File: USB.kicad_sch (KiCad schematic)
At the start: 8 parts, among them J3 USB-C_GCT_USB4145-03-0070-C, U11 TPD4E05U06QDQARQ1

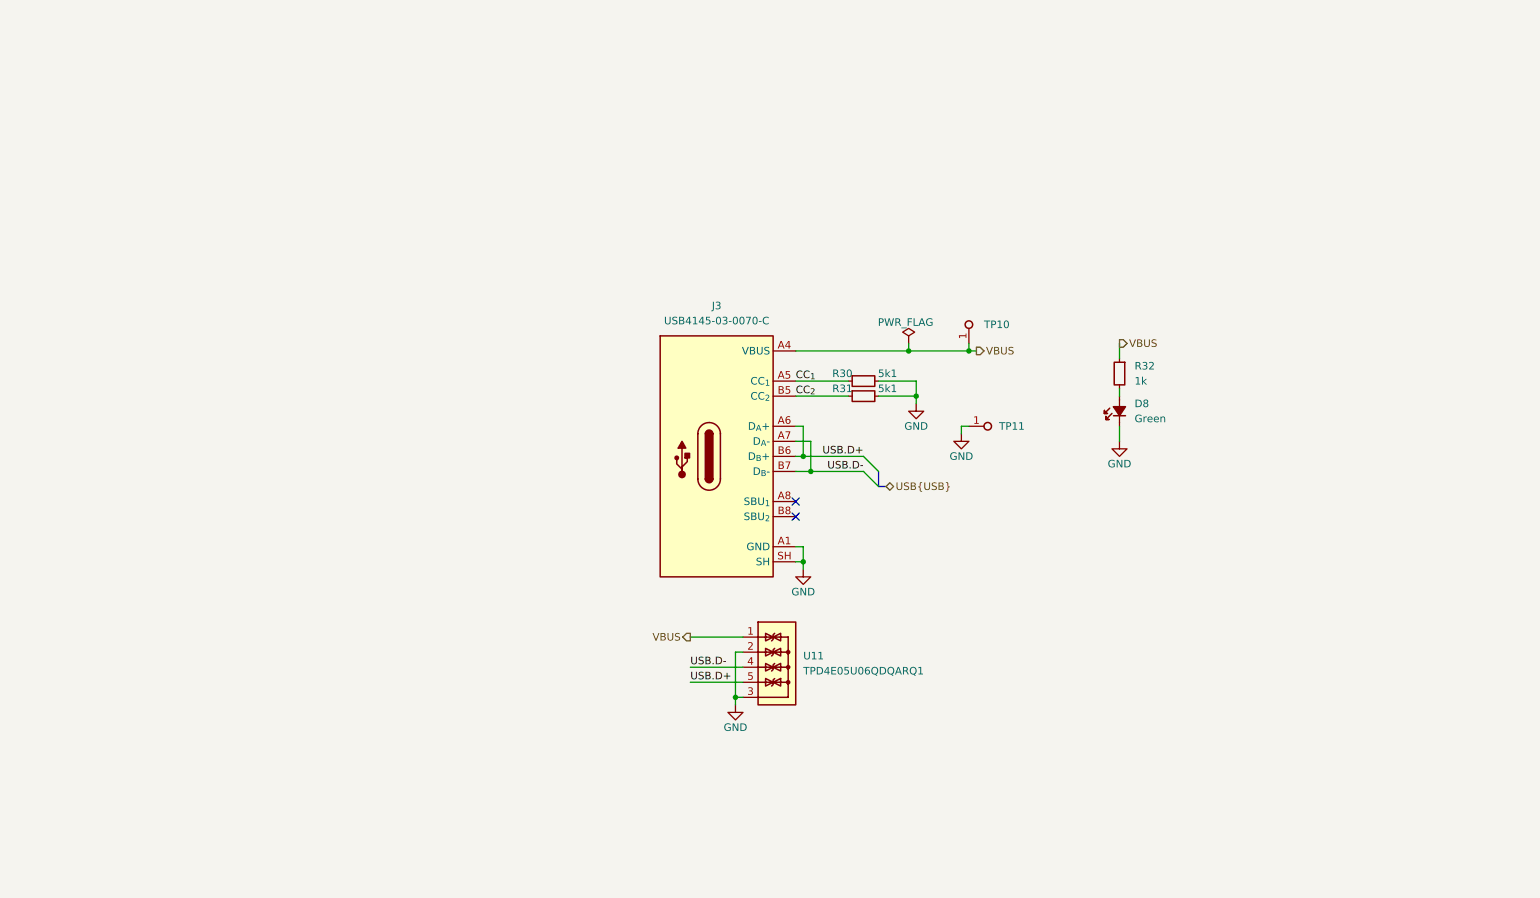
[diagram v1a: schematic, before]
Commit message: [#72133] Update USB FTDI sheet
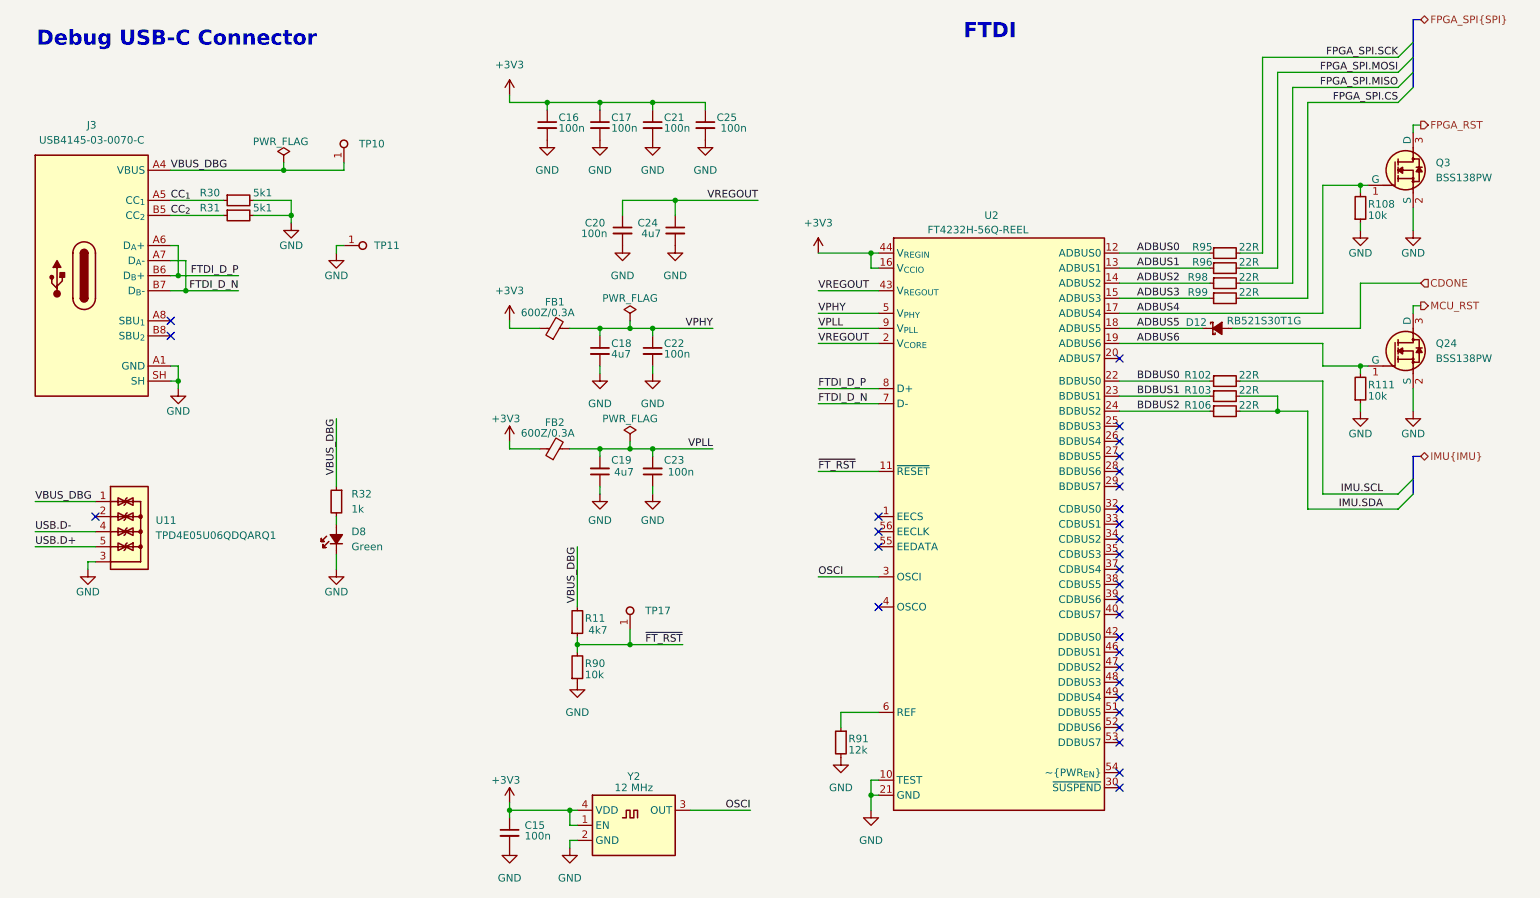
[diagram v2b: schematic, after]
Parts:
- added C15, C16, C17, C20, C21, C22, C23, C25: C_100n_16V_X7R_0402, antmicro-footprints:C_0402_1005Metric, symbol antmicroCapacitors0402:C_100n_16V_X7R_0402
- added C18, C19, C24: C_4u7_0402, antmicro-footprints:C_0402_1005Metric, symbol antmicroCapacitors0402:C_4u7_0402
- added D12: RB521S30T1G, antmicro-footprints:SOD-523, symbol antmicroDiodesRectifiersSingle:RB521S30T1G
- added FB1, FB2: FB_600Z_0.3A_Murata-BLM15AG_0402, antmicro-footprints:FB_0402_1005Metric, symbol antmicroFerriteBeadsandChips:FB_600Z_0.3A_Murata-BLM15AG_0402
- added Q24, Q3: BSS138PW, antmicro-footprints:SC70-3, symbol antmicroTransistorsFETsMOSFETsSingle:BSS138PW
- added R102, R103, R106, R95, R96, R98, R99: R_22R_0402, antmicro-footprints:R_0402_1005Metric, symbol antmicroResistors0402:R_22R_0402
- added R108, R111, R90: R_10k_0402, antmicro-footprints:R_0402_1005Metric, symbol antmicroResistors0402:R_10k_0402
- added R11: R_4k7_0402, antmicro-footprints:R_0402_1005Metric, symbol antmicroResistors0402:R_4k7_0402
- added R91: R_12k_0402, antmicro-footprints:R_0402_1005Metric, symbol antmicroResistors0402:R_12k_0402
- added TP17: TP_0.75mm_SMD, antmicro-footprints:TP_SMD_0.75mm, symbol antmicroTestPoints:TP_0.75mm_SMD
- added U2: FT4232H_VQFN, antmicro-footprints:QFN-56-1EP_8x8mm_P0.5mm, symbol antmicroInterfaceControllers:FT4232H_VQFN
- added Y2: Oscillator_12MHz_ASFLMB, antmicro-footprints:Oscillator_SMD_Abracon_ASFLMB_5x3.2x0.85mm, symbol antmicroOscillators:Oscillator_12MHz_ASFLMB
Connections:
- net GND: now also C15.2, C16.2, C17.2, C18.2, C19.1, C20.2, C21.2, C22.2, C23.1, C24.2, C25.2, Q24.2 (S), Q3.2 (S), R108.1, R111.1, R90.1, R91.2, U2.10 (TEST), U2.21 (GND), U2.41 (GND), U2.45 (GND), U2.57 (GND), Y2.2 (GND); no longer U11.2, U11.9
- net USB.D+: no longer J3.A6 (D_{A}+), J3.B6 (D_{B}+)
- net USB.D-: no longer J3.A7 (D_{A}-), J3.B7 (D_{B}-)
- net VBUS renamed VBUS_DBG
- net VBUS_DBG: now also R11.2
- new net: R91.1, U2.6 (REF)
- new net: U11.2, U11.9
- new net +3V3: C15.1, C16.1, C17.1, C21.1, C25.1, FB1.1, FB2.1, U2.16 (V_{CCIO}), U2.36 (V_{CCIO}), U2.44 (V_{REGIN}), U2.50 (V_{CCIO}), Y2.1 (EN), Y2.4 (VDD)
- new net ADBUS0: R95.1, U2.12 (ADBUS0)
- new net ADBUS1: R96.1, U2.13 (ADBUS1)
- new net ADBUS2: R98.1, U2.14 (ADBUS2)
- new net ADBUS3: R99.1, U2.15 (ADBUS3)
- new net ADBUS4: Q3.1 (G), R108.2, U2.17 (ADBUS4)
- new net ADBUS5: D12.1 (C), U2.18 (ADBUS5)
- new net ADBUS6: Q24.1 (G), R111.2, U2.19 (ADBUS6)
- new net BDBUS0: R102.1, U2.22 (BDBUS0)
- new net BDBUS1: R103.1, U2.23 (BDBUS1)
- new net BDBUS2: R106.1, U2.24 (BDBUS2)
- new net CDONE: D12.2 (A)
- new net FPGA_RST: Q3.3 (D)
- new net FPGA_SPI.CS: R99.2
- new net FPGA_SPI.MISO: R98.2
- new net FPGA_SPI.MOSI: R96.2
- new net FPGA_SPI.SCK: R95.2
- new net FTDI_D_N: J3.A7 (D_{A}-), J3.B7 (D_{B}-), U2.7 (D-)
- new net FTDI_D_P: J3.A6 (D_{A}+), J3.B6 (D_{B}+), U2.8 (D+)
- new net IMU.SCL: R102.2
- new net IMU.SDA: R103.2, R106.2
- new net MCU_RST: Q24.3 (D)
- new net OSCI: U2.3 (OSCI), Y2.3 (OUT)
- new net VPHY: C18.1, C22.1, FB1.2, U2.5 (V_{PHY})
- new net VPLL: C19.2, C23.2, FB2.2, U2.9 (V_{PLL})
- new net VREGOUT: C20.1, C24.1, U2.2 (V_{CORE}), U2.31 (V_{CORE}), U2.43 (V_{REGOUT})
- new net ~{FT_RST}: R11.1, R90.2, TP17.1, U2.11 (~{RESET})
- no-connect marks 2 -> 31
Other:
- note added: "Debug USB-C Connector"
- note added: "FTDI"
- moved on the sheet: D8, J3, R30, R31, R32, TP10, TP11, U11

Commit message: [#72133] Update USB sheets
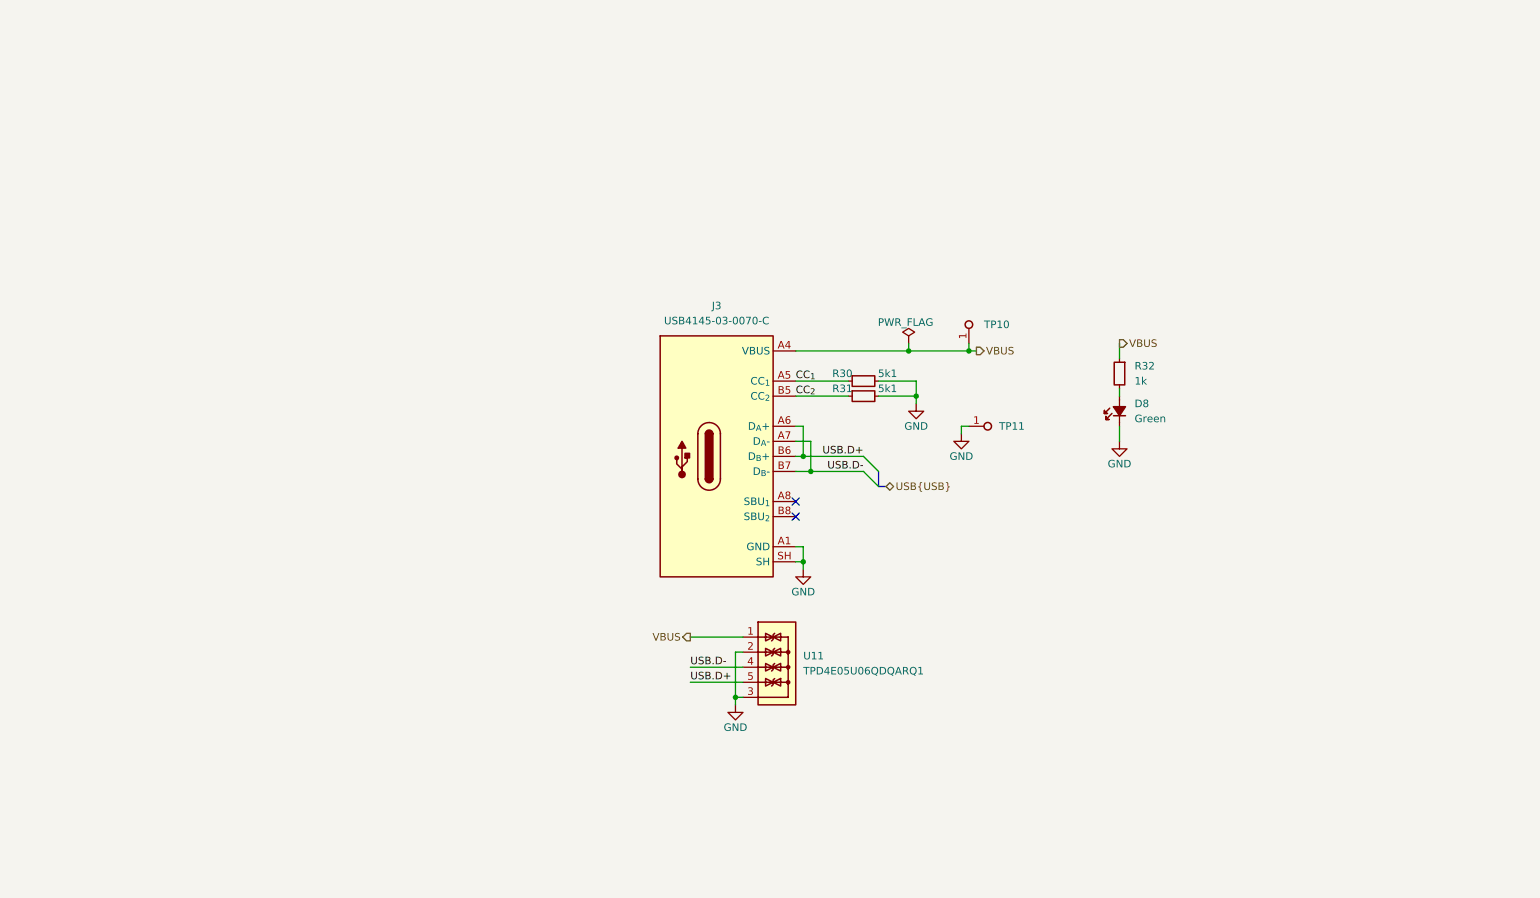
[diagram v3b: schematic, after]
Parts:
- removed C15, C16, C17, C20, C21, C22, C23, C25: C_100n_16V_X7R_0402, antmicro-footprints:C_0402_1005Metric, symbol antmicroCapacitors0402:C_100n_16V_X7R_0402
- removed C18, C19, C24: C_4u7_0402, antmicro-footprints:C_0402_1005Metric, symbol antmicroCapacitors0402:C_4u7_0402
- removed D12: RB521S30T1G, antmicro-footprints:SOD-523, symbol antmicroDiodesRectifiersSingle:RB521S30T1G
- removed FB1, FB2: FB_600Z_0.3A_Murata-BLM15AG_0402, antmicro-footprints:FB_0402_1005Metric, symbol antmicroFerriteBeadsandChips:FB_600Z_0.3A_Murata-BLM15AG_0402
- removed Q24, Q3: BSS138PW, antmicro-footprints:SC70-3, symbol antmicroTransistorsFETsMOSFETsSingle:BSS138PW
- removed R102, R103, R106, R95, R96, R98, R99: R_22R_0402, antmicro-footprints:R_0402_1005Metric, symbol antmicroResistors0402:R_22R_0402
- removed R108, R111, R90: R_10k_0402, antmicro-footprints:R_0402_1005Metric, symbol antmicroResistors0402:R_10k_0402
- removed R11: R_4k7_0402, antmicro-footprints:R_0402_1005Metric, symbol antmicroResistors0402:R_4k7_0402
- removed R91: R_12k_0402, antmicro-footprints:R_0402_1005Metric, symbol antmicroResistors0402:R_12k_0402
- removed TP17: TP_0.75mm_SMD, antmicro-footprints:TP_SMD_0.75mm, symbol antmicroTestPoints:TP_0.75mm_SMD
- removed U2: FT4232H_VQFN, antmicro-footprints:QFN-56-1EP_8x8mm_P0.5mm, symbol antmicroInterfaceControllers:FT4232H_VQFN
- removed Y2: Oscillator_12MHz_ASFLMB, antmicro-footprints:Oscillator_SMD_Abracon_ASFLMB_5x3.2x0.85mm, symbol antmicroOscillators:Oscillator_12MHz_ASFLMB
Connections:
- net FTDI_D_N is gone; now on net USB.D-: J3.A7 (D_{A}-), J3.B7 (D_{B}-)
- net FTDI_D_P is gone; now on net USB.D+: J3.A6 (D_{A}+), J3.B6 (D_{B}+)
- net GND: now also U11.2, U11.9
- net VBUS_DBG renamed VBUS
- no-connect marks 31 -> 2
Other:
- note removed: "Debug USB-C Connector"
- note removed: "FTDI"
- moved on the sheet: D8, J3, R30, R31, R32, TP10, TP11, U11

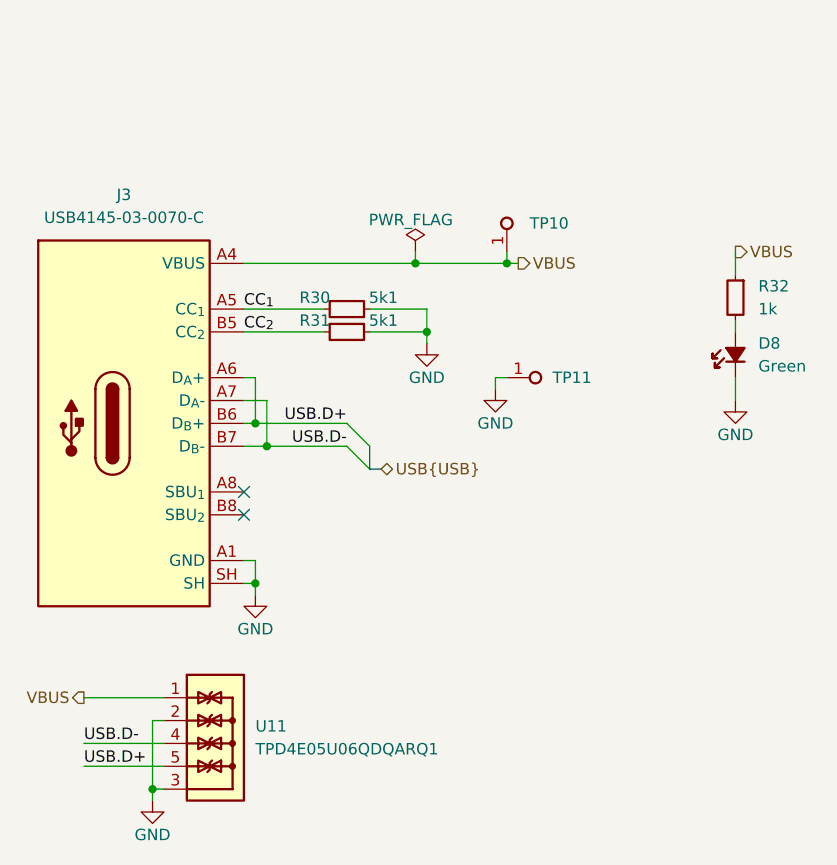
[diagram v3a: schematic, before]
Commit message: [#72133] Add captions to schematic sheets
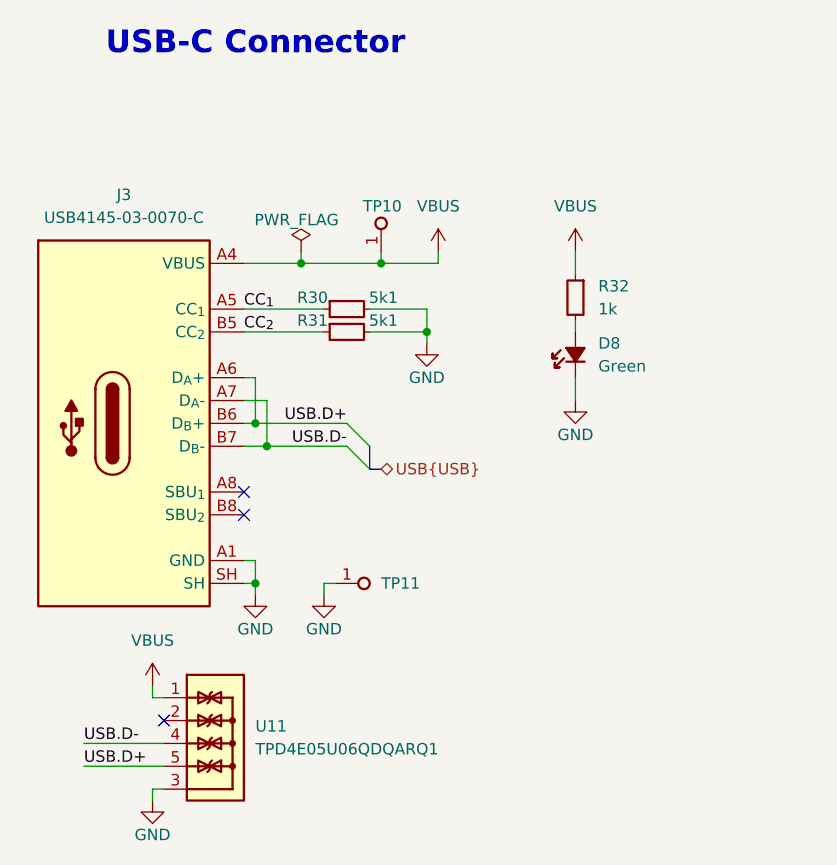
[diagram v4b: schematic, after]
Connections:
- net GND: no longer U11.2, U11.9
- new net: U11.2, U11.9
- no-connect marks 2 -> 3
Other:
- note added: "USB-C Connector"
- moved on the sheet: D8, R32, TP10, TP11

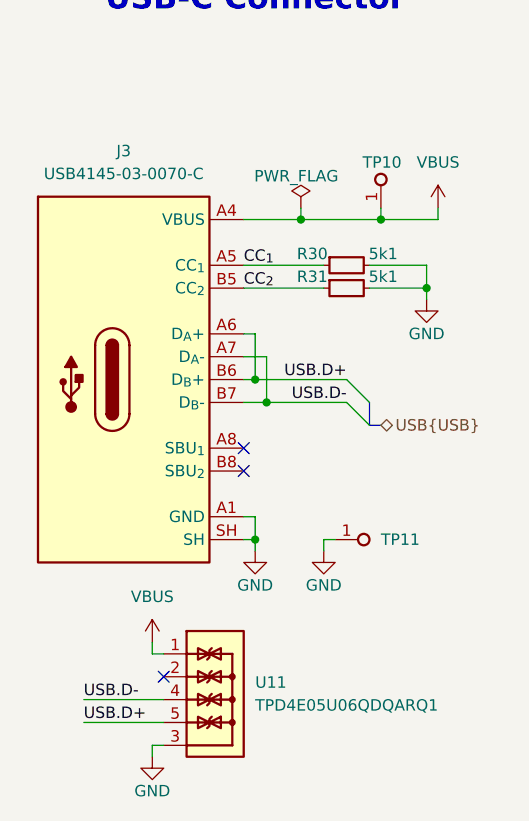
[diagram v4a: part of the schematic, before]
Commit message: [#72447] Change connectors to horizontal
Signed-off-by: Dawid Lentka <dlentka@antmicro.com>
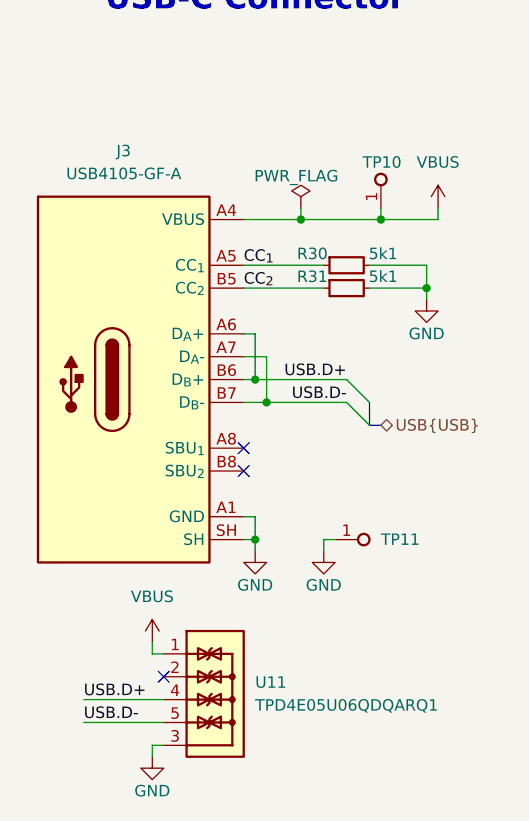
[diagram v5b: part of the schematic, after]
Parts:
- J3: value USB-C_GCT_USB4145-03-0070-C -> USB-C_GCT_USB4105-GF-A; footprint antmicro-footprints:USB-C_Receptacle_GCT_USB4145-03-0070-C -> antmicro-footprints:USB-C_Receptacle_GCT_USB4105-GF-A; symbol antmicroUSBConnectors:USB-C_GCT_USB4145-03-0070-C -> antmicroUSBConnectors:USB-C_GCT_USB4105-GF-A; MPN USB4145-03-0070-C -> USB4105-GF-A
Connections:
- net USB.D+: now also U11.4, U11.7; no longer U11.5, U11.6
- net USB.D-: now also U11.5, U11.6; no longer U11.4, U11.7
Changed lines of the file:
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@@
 	)
 	(label "USB.D+"
-		(at 132.08 130.81 0)
+		(at 132.08 128.27 0)
 		(fields_autoplaced yes)
 		(effects
@@
 	)
 	(label "USB.D-"
-		(at 132.08 128.27 0)
+		(at 132.08 130.81 0)
 		(fields_autoplaced yes)
 		(effects
@@
 	)
 	(symbol
-		(lib_id "antmicroUSBConnectors:USB-C_GCT_USB4145-03-0070-C")
+		(lib_id "antmicroUSBConnectors:USB-C_GCT_USB4105-GF-A")
 		(at 149.86 74.93 0)
 		(unit 1)
@@
 			)
 		)
-		(property "Value" "USB-C_GCT_USB4145-03-0070-C"
+		(property "Value" "USB-C_GCT_USB4105-GF-A"
 			(at 136.525 69.85 0)
 			(effects
@@
 			)
 		)
-		(property "Footprint" "antmicro-footprints:USB-C_Receptacle_GCT_USB4145-03-0070-C"
+		(property "Footprint" "antmicro-footprints:USB-C_Receptacle_GCT_USB4105-GF-A"
 			(at 171.45 85.09 0)
 			(effects
@@
 			)
 		)
-		(property "Datasheet" "https://gct.co/files/drawings/usb4145.pdf"
+		(property "Datasheet" "https://gct.co/files/drawings/usb4105.pdf"
 			(at 171.45 87.63 0)
 			(effects
@@
 			)
 		)
-		(property "Description" "USB-C (USB TYPE-C) USB 2.0 Receptacle Connector 24 (16+8 Dummy) Postion  Surface Mount, Vertical"
+		(property "Description" "USB-C (USB TYPE-C) USB 2.0 Receptacle Connector 24 (16+8 Dummy) Position Surface Mount, Right Angle"
 			(at 149.86 74.93 0)
 			(effects
@@
 			)
 		)
-		(property "MPN" "USB4145-03-0070-C"
+		(property "MPN" "USB4105-GF-A"
 			(at 136.525 69.85 0)
 			(effects

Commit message: Bump to KiCad 9.x
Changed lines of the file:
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@@
 (kicad_sch
-	(version 20231120)
+	(version 20250114)
 	(generator "eeschema")
-	(generator_version "8.0")
+	(generator_version "9.0")
 	(paper "A4")
 	(title_block
@@
 		(rev "1.0.0")
 	)
+	(text "USB-C Connector"
+		(exclude_from_sim no)
+		(at 151.13 50.546 0)
+		(effects
+			(font
+				(size 2.54 2.54)
+				(thickness 0.508)
+				(bold yes)
+			)
+		)
+	)
 	(junction
 		(at 151.13 110.49)
@@
 		)
 	)
-	(text "USB-C Connector"
-		(exclude_from_sim no)
-		(at 151.13 50.546 0)
-		(effects
-			(font
-				(size 2.54 2.54)
-				(thickness 0.508)
-				(bold yes)
-			)
-		)
-	)
 	(label "USB.D+"
 		(at 132.08 128.27 0)
-		(fields_autoplaced yes)
 		(effects
 			(font
@@
 	(label "USB.D-"
 		(at 132.08 130.81 0)
-		(fields_autoplaced yes)
 		(effects
 			(font
@@
 	(label "CC_{1}"
 		(at 149.86 80.01 0)
-		(fields_autoplaced yes)
 		(effects
 			(font
@@
 	(label "USB.D-"
 		(at 161.29 95.25 180)
-		(fields_autoplaced yes)
 		(effects
 			(font
@@
 	(label "CC_{2}"
 		(at 149.86 82.55 0)
-		(fields_autoplaced yes)
 		(effects
 			(font
@@
 	(label "USB.D+"
 		(at 161.29 92.71 180)
-		(fields_autoplaced yes)
 		(effects
 			(font
@@
 		(shape bidirectional)
 		(at 165.1 97.79 0)
-		(fields_autoplaced yes)
-		(effects
-			(font
+		(effects
+			(font
